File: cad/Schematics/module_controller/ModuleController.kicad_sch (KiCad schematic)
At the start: 24 parts, among them J1 JST B5B-XH-A, J6 2x08 Edge Connector, U1 ULN2003, U2 A1101xLH, U3 SN75176AP, U4 ATmega8A-A, Y1 16,0000-HC49U-S

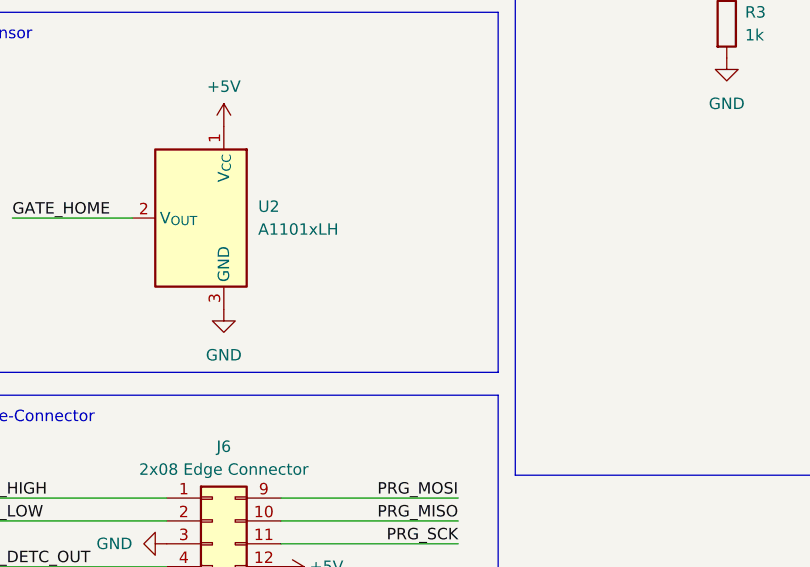
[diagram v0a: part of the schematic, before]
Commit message: add print profiles and update schematics
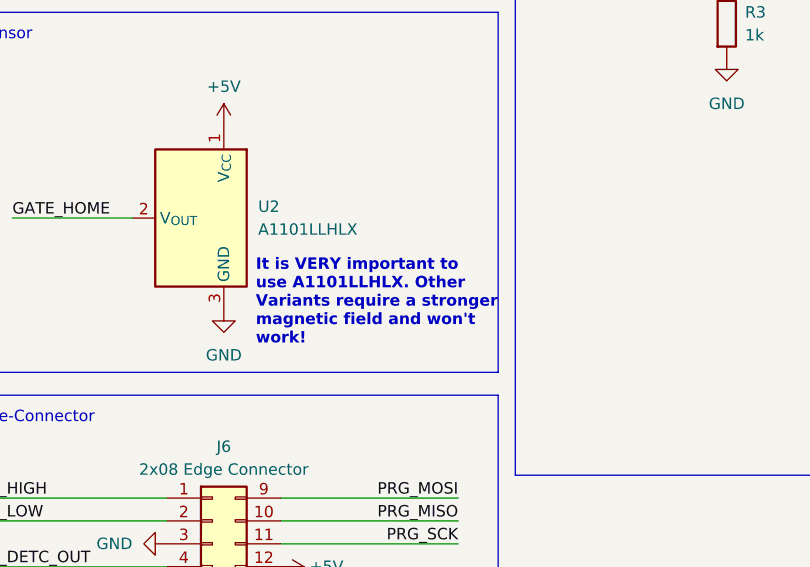
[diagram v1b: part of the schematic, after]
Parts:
- U2: value A1101xLH -> A1101LLHLX
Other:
- note added: "It is VERY important to use A1101LLHLX. Other Variants require a stronger magnetic field and won't work!"
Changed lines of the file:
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@@
+		)
+	)
+	(text "It is VERY important to \nuse A1101LLHLX. Other\nVariants require a stronger\nmagnetic field and won't\nwork!"
+		(exclude_from_sim no)
+		(at 63.246 140.208 0)
+		(effects
+			(font
+				(size 1.27 1.27)
+				(thickness 0.254)
+				(bold yes)
+				(color 255 0 45 1)
+			)
+			(justify left)
 		)
 	)
@@
 			)
 		)
-		(property "Value" "A1101xLH"
+		(property "Value" "A1101LLHLX"
 			(at 63.5 132.0799 0)
 			(effects

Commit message: update schematics annotation
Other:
- note added: "It is VERY important to use A1101LLHL*. Other Variants require a stronger magnetic field and won't work!"
- note removed: "It is VERY important to use A1101LLHLX. Other Variants require a stronger magnetic field and won't work!"
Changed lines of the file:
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@@
 		)
 	)
-	(text "It is VERY important to \nuse A1101LLHLX. Other\nVariants require a stronger\nmagnetic field and won't\nwork!"
+	(text "It is VERY important to \nuse A1101LLHL*. Other\nVariants require a stronger\nmagnetic field and won't\nwork!"
 		(exclude_from_sim no)
 		(at 63.246 140.208 0)
